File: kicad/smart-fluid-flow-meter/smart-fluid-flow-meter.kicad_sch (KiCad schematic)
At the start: 7 parts, among them J1 YF-S201, SW1 Factory reset button, U1 ESP32-WROOM-32

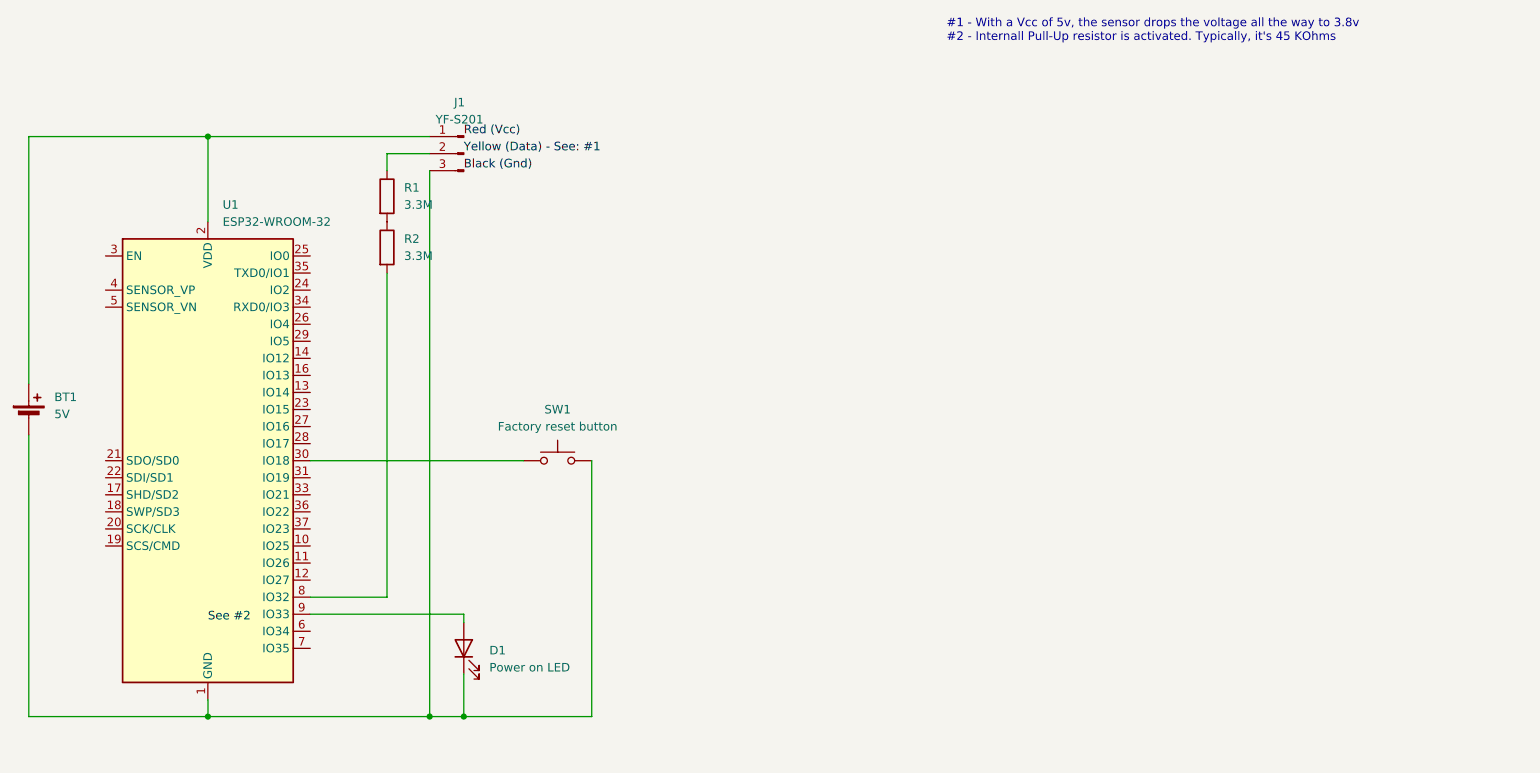
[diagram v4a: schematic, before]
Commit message: Turn on power LED
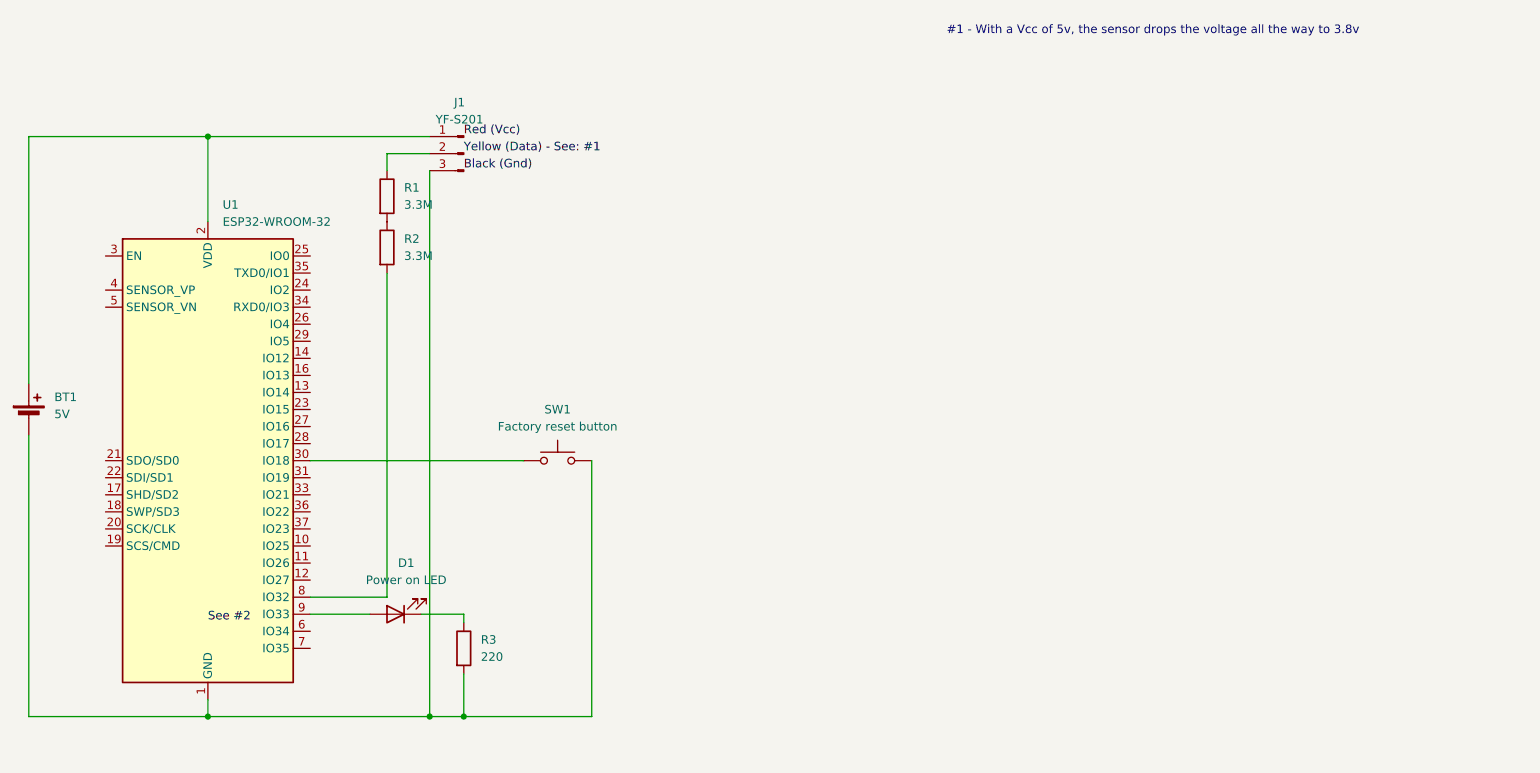
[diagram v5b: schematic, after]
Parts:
- added R3: 220, symbol Device:R
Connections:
- net at BT1.2 (-), J1.3 (Pin_3), SW1.2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: now also R3.2; no longer D1.1 (K)
- new net: D1.1 (K), R3.1
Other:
- note added: "#1 - With a Vcc of 5v, the sensor drops the voltage all the way to 3.8v"
- note removed: "#1 - With a Vcc of 5v, the sensor drops the voltage all the way to 3.8v #2 - Internall Pull-Up resistor is activated. Typically, it's 45 KOhms"
- moved on the sheet: D1
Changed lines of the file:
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@@
+	(wire
+		(pts
+			(xy 132.08 105.41) (xy 138.43 105.41)
+		)
+		(stroke
+			(width 0)
+			(type default)
+		)
+	)
 	(wire
 		(pts
@@
 	(wire
 		(pts
-			(xy 115.57 105.41) (xy 138.43 105.41)
+			(xy 115.57 105.41) (xy 124.46 105.41)
 		)
 		(stroke
@@
 		)
 	)
-	(text "#1 - With a Vcc of 5v, the sensor drops the voltage all the way to 3.8v\n#2 - Internall Pull-Up resistor is activated. Typically, it's 45 KOhms"
+	(text "#1 - With a Vcc of 5v, the sensor drops the voltage all the way to 3.8v"
 		(exclude_from_sim no)
 		(at 210.312 18.542 0)
@@
 	(symbol
 		(lib_id "Device:LED")
-		(at 138.43 110.49 90)
+		(at 128.27 105.41 180)
 		(unit 1)
 		(exclude_from_sim no)
@@
 		(fields_autoplaced yes)
 		(property "Reference" "D1"
-			(at 142.24 110.8074 90)
-			(effects
-				(font
-					(size 1.27 1.27)
-				)
-				(justify right)
+			(at 129.8575 97.79 0)
+			(effects
+				(font
+					(size 1.27 1.27)
+				)
 			)
 		)
 		(property "Value" "Power on LED"
-			(at 142.24 113.3474 90)
-			(effects
-				(font
-					(size 1.27 1.27)
-				)
-				(justify right)
+			(at 129.8575 100.33 0)
+			(effects
+				(font
+					(size 1.27 1.27)
+				)
 			)
 		)
 		(property "Footprint" ""
-			(at 138.43 110.49 0)
+			(at 128.27 105.41 0)
 			(effects
 				(font
@@
 		)
 		(property "Datasheet" "~"
-			(at 138.43 110.49 0)
+			(at 128.27 105.41 0)
 			(effects
 				(font
@@
 		)
 		(property "Description" "Light emitting diode"
-			(at 138.43 110.49 0)
+			(at 128.27 105.41 0)
 			(effects
 				(font
@@
 					(unit 1)
 				)
+			)
+		)
+	)
+	(symbol
+		(lib_id "Device:R")
+		(at 138.43 110.49 0)
+		(unit 1)
+		(exclude_from_sim no)
+		(in_bom yes)
+		(on_board yes)
+		(dnp no)
+		(fields_autoplaced yes)
+		(property "Reference" "R3"
+			(at 140.97 109.2199 0)
+			(effects
+				(font
+					(size 1.27 1.27)
+				)
+				(justify left)
+			)
+		)
+		(property "Value" "220"
+			(at 140.97 111.7599 0)
+			(effects
+				(font
+					(size 1.27 1.27)
+				)
+				(justify left)
+			)
+		)
+		(property "Footprint" ""
+			(at 136.652 110.49 90)
+			(effects
+				(font
+					(size 1.27 1.27)
+				)
+				(hide yes)
+			)
+		)
+		(property "Datasheet" "~"
+			(at 138.43 110.49 0)
+			(effects
+				(font
+					(size 1.27 1.27)
+				)
+				(hide yes)
+			)
+		)
+		(property "Description" "Resistor"
+			(at 138.43 110.49 0)
+			(effects
+				(font
+					(size 1.27 1.27)
+				)
+				(hide yes)
+			)
+		)
+		(pin "1"
+		)
+		(pin "2"
+		)
+		(instances
+			(project ""
+				(path "/39fefc38-68db-426d-adc7-52db70b33c24"
+					(reference "R3")
+					(unit 1)
+				)

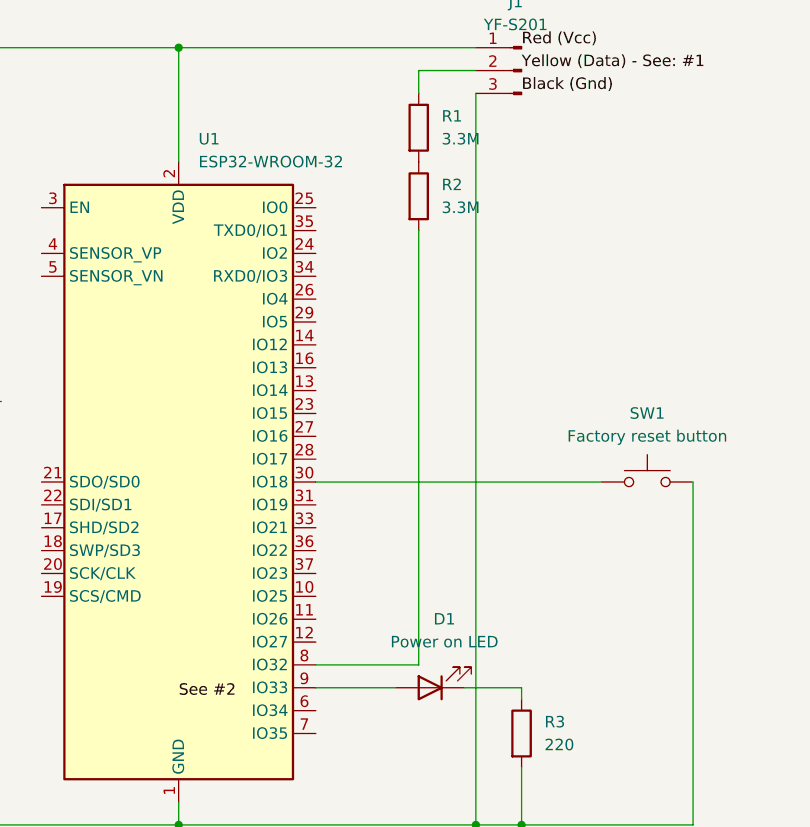
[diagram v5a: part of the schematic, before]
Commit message: [esp32] Read measurements from flow meter (#62)
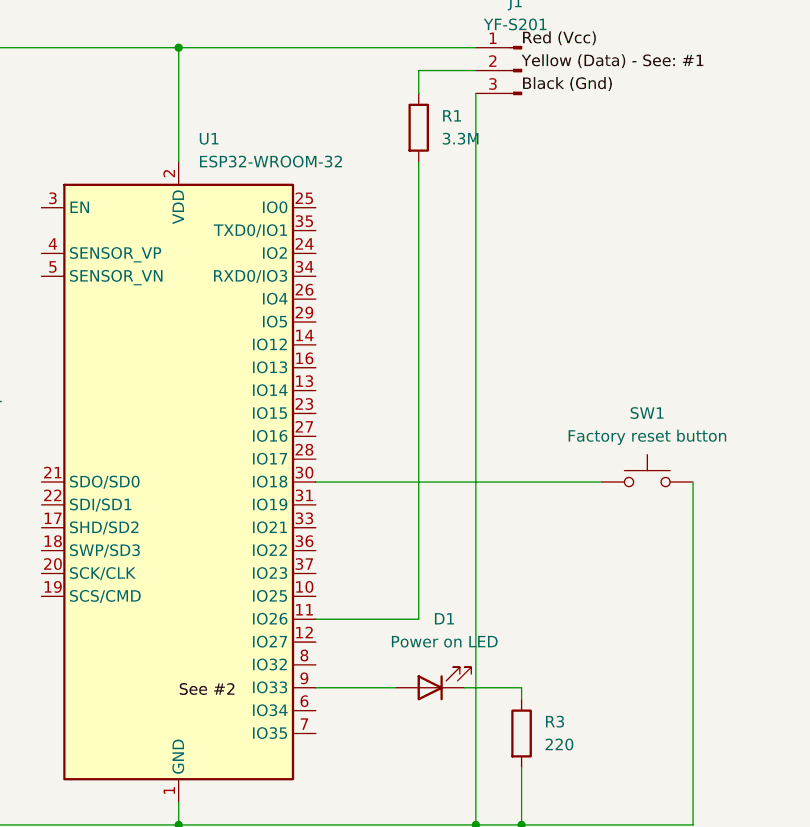
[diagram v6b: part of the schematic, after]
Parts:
- removed R2: 3.3M, symbol Device:R
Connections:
- net at U1.11 (IO26): now also R1.2
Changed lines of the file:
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@@
 	(wire
 		(pts
-			(xy 127 54.61) (xy 127 102.87)
+			(xy 115.57 97.79) (xy 127 97.79)
 		)
 		(stroke
@@
 	(wire
 		(pts
-			(xy 115.57 102.87) (xy 127 102.87)
-		)
-		(stroke
-			(width 0)
-			(type default)
-		)
-	)
-	(wire
-		(pts
 			(xy 138.43 120.65) (xy 157.48 120.65)
+		)
+		(stroke
+			(width 0)
+			(type default)
+		)
+	)
+	(wire
+		(pts
+			(xy 127 46.99) (xy 127 97.79)
 		)
 		(stroke
@@
 					(unit 1)
 				)
-			)
-		)
-	)
-	(symbol
-		(lib_id "Device:R")
-		(at 127 50.8 0)
-		(unit 1)
-		(exclude_from_sim no)
-		(in_bom yes)
-		(on_board yes)
-		(dnp no)
-		(fields_autoplaced yes)
-		(property "Reference" "R2"
-			(at 129.54 49.5299 0)
-			(effects
-				(font
-					(size 1.27 1.27)
-				)
-				(justify left)
-			)
-		)
-		(property "Value" "3.3M"
-			(at 129.54 52.0699 0)
-			(effects
-				(font
-					(size 1.27 1.27)
-				)
-				(justify left)
-			)
-		)
-		(property "Footprint" ""
-			(at 125.222 50.8 90)
-			(effects
-				(font
-					(size 1.27 1.27)
-				)
-				(hide yes)
-			)
-		)
-		(property "Datasheet" "~"
-			(at 127 50.8 0)
-			(effects
-				(font
-					(size 1.27 1.27)
-				)
-				(hide yes)
-			)
-		)
-		(property "Description" "Resistor"
-			(at 127 50.8 0)
-			(effects
-				(font
-					(size 1.27 1.27)
-				)
-				(hide yes)
-			)
-		)
-		(pin "1"
-		)
-		(pin "2"
-		)
-		(instances
-			(project "smart-fluid-flow-meter"
-				(path "/39fefc38-68db-426d-adc7-52db70b33c24"
-					(reference "R2")
-					(unit 1)
-				)

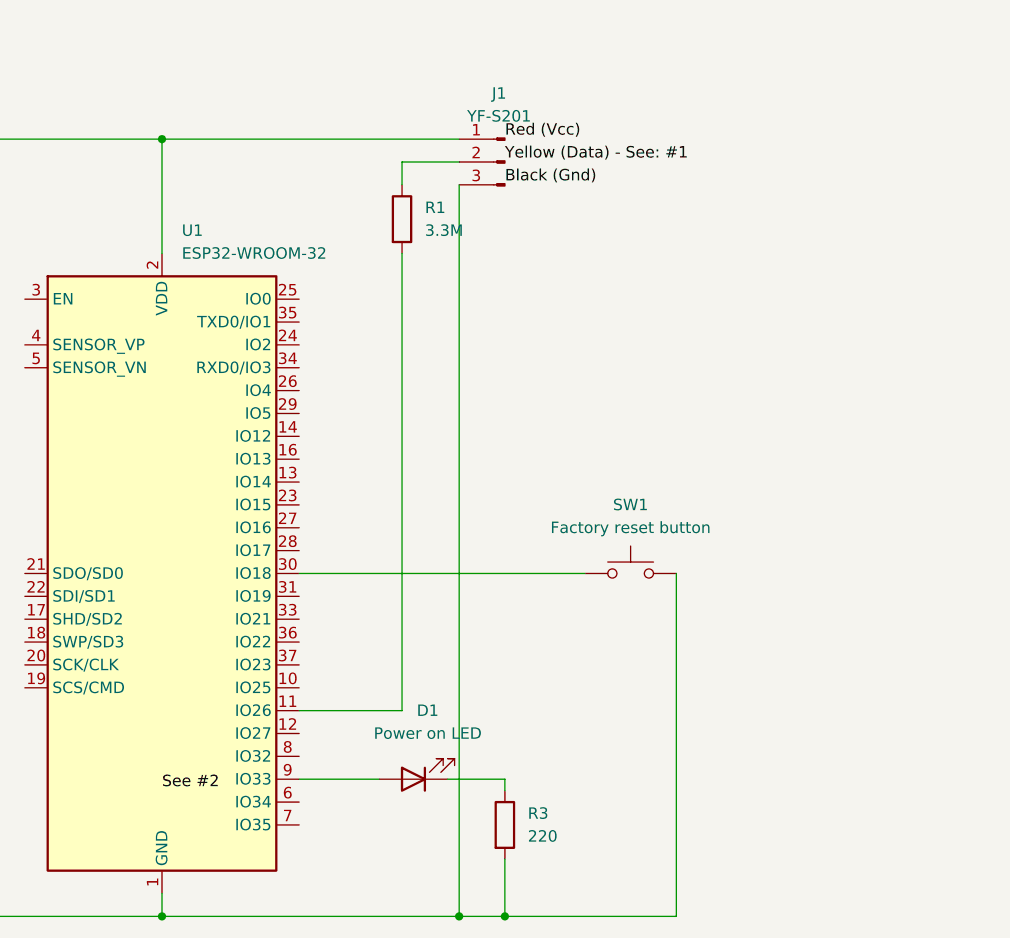
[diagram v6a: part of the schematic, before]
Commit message: Add status LEDs to kicad. #26 (#70)
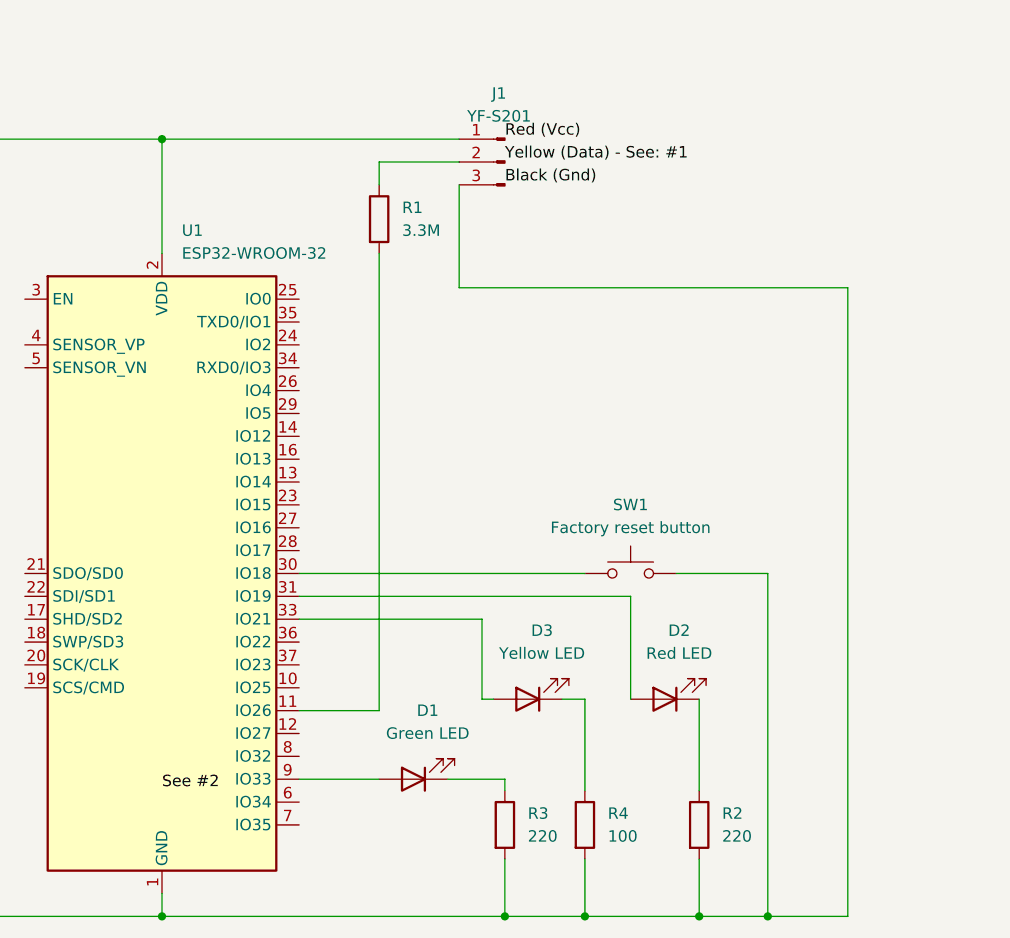
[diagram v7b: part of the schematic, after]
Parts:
- added D2: Red LED, symbol Device:LED
- added D3: Yellow LED, symbol Device:LED
- added R2: 220, symbol Device:R
- added R4: 100, symbol Device:R
- D1: value Power on LED -> Green LED
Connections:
- net at BT1.2 (-), J1.3 (Pin_3), R3.2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: now also R2.2, R4.2
- net at U1.31 (IO19): now also D2.2 (A)
- net at U1.33 (IO21): now also D3.2 (A)
- new net: D3.1 (K), R4.1
- new net: D2.1 (K), R2.1
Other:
- moved on the sheet: R1

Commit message: Add spice model propererties to some symbols
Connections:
- net 0: now reaches BT1.2 (-), J1.3 (Pin_3), R2.2, R3.2, R4.2, SW1.2, U1.1 (GND), U1.15 (GND), U1.38 (GND), U1.39 (GND)
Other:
- note removed: "#1 - With a Vcc of 5v, the sensor drops the voltage all the way to 3.8v"
